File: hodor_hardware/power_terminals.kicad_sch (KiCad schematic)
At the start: 60 parts, among them J1 Screw_Terminal_01x02, Q1 SiS443DN, T1 GND, T10 V_{BUS}, T11 3V3, T12 5V, T14 V_{BUS}_SENSE, T32 GND, T6 V_{DC}_SENSE, T9 V_{DC}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

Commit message: Schematic finished
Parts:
- removed C62: 100n, Capacitor_SMD:C_0402_1005Metric, symbol Device:C
- added C66, C67, C68, C69, C70: 10uF, Capacitor_SMD:C_0805_2012Metric, symbol Device:C
- C10, C38, C58, C65: value 100n -> 100nF
- C45: value 100n -> 4.7uF/50V; footprint Capacitor_SMD:C_0402_1005Metric -> Capacitor_SMD:C_1206_3216Metric
- C46, C59: value 100n -> 100n/50V; footprint Capacitor_SMD:C_0402_1005Metric -> Capacitor_SMD:C_0603_1608Metric
- C57: value 100n -> 6.8nF
- C60: value 100n -> 15nF
- C61: value 100n -> 10p
- C64: footprint Capacitor_SMD:C_1206_3216Metric -> Capacitor_SMD:C_0805_2012Metric
- D16: value D_Schottky -> PMEG4050; footprint (none) -> Diode_SMD:D_SMB
- L13: value L_Iron -> 27uH; footprint (none) -> Inductor_SMD:L_12x12mm_H6mm
- R22, R42: value 2k -> 2.2k
- R41: value 18.2k -> 100k
- R73: value 18.2k -> 52.3k
- R74: value 18.2k -> 10k
- R75: value 18.2k -> 205k
- T1, T10, T11, T12, T14, T32, T6, T9: now left out of the parts list
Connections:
- net +5V: now also C66.1, C67.1, C68.1, C69.1, C70.1
- net GND: now also C66.2, C67.2, C68.2, C69.2, C70.2
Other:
- note added: "DC/DC converters for logic supply"
- note removed: "WARNING: R/C Values not calculated yet!"
- moved on the sheet: C45, C46, C57, C58, C59, C60, C61, C63, C64, C65, D16, L13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

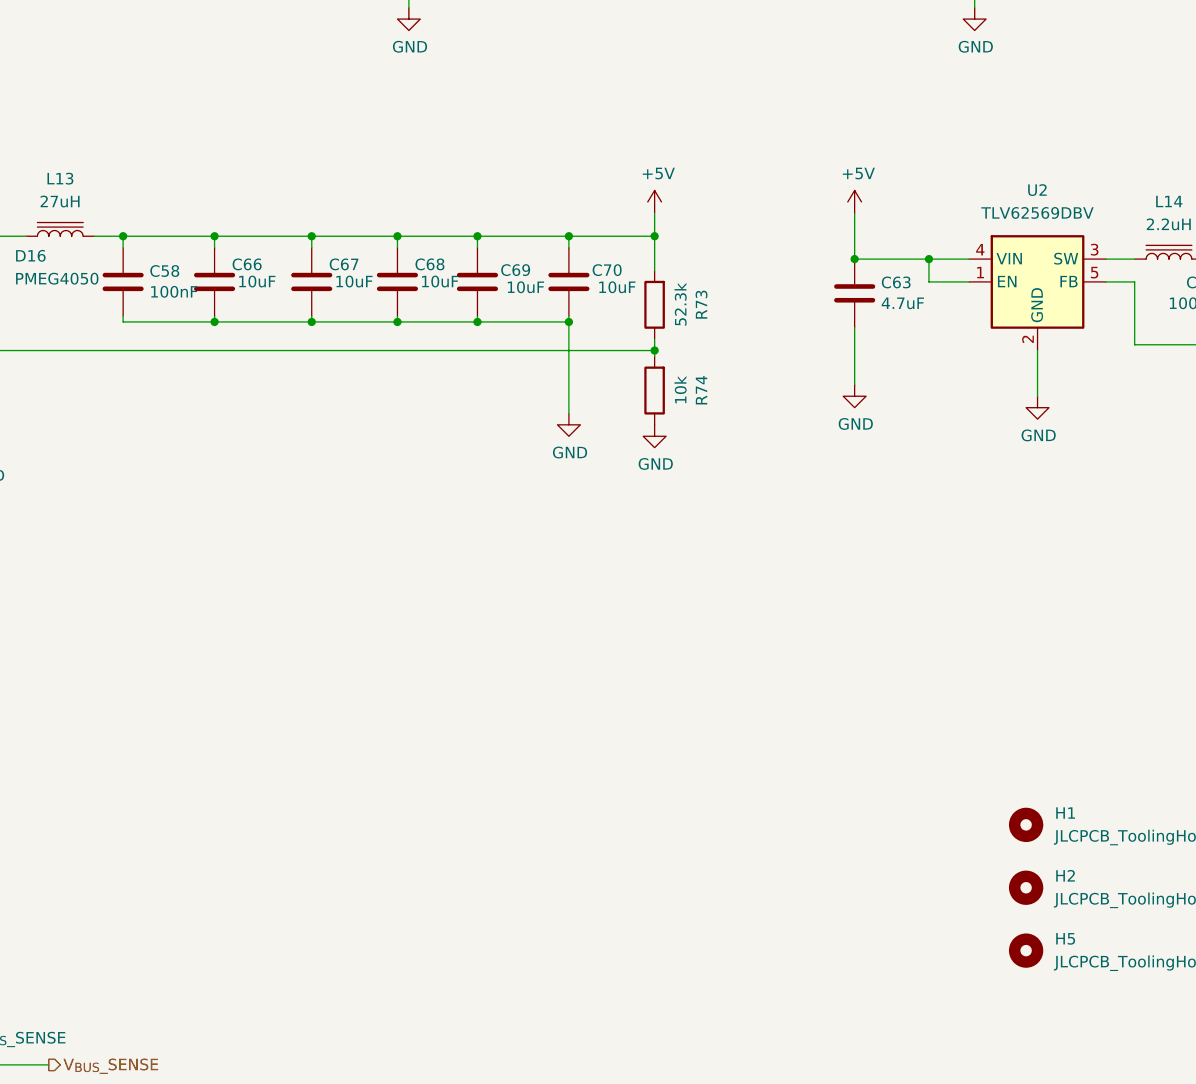
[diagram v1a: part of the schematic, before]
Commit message: Added USB switchover function for 5V
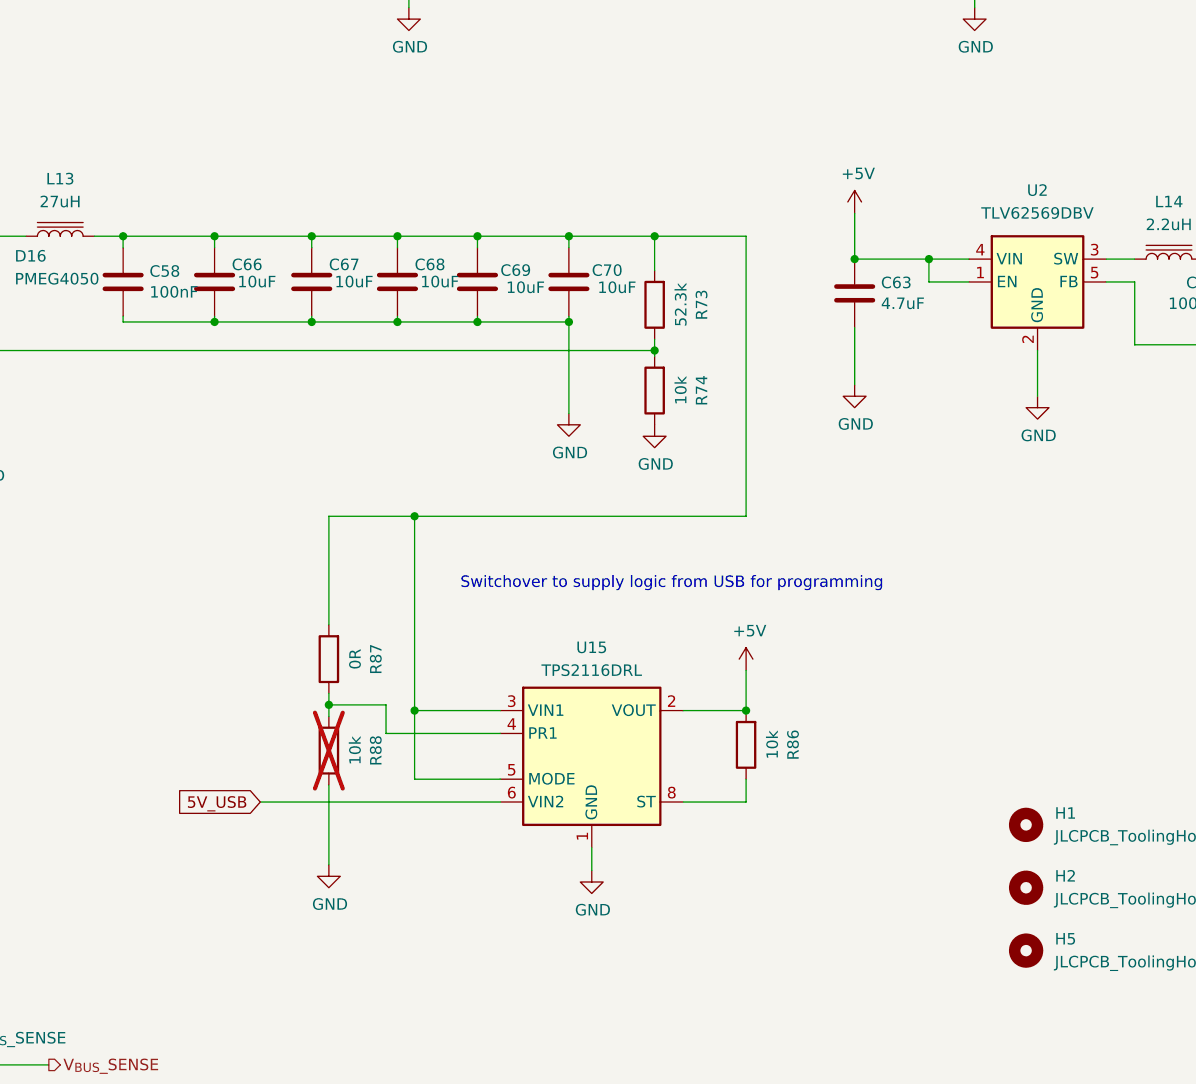
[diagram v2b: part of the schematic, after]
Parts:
- added R86, R88: 10k, Resistor_SMD:R_0402_1005Metric, symbol Device:R
- added R87: 0R, Resistor_SMD:R_0402_1005Metric, symbol Device:R
- added U15: TPS2116DRL, Package_TO_SOT_SMD:SOT-583-8, symbol Power_Management:TPS2116DRL
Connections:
- net +5V: now also R86.2, U15.2 (VOUT), U15.7 (VOUT); no longer C58.1, C66.1, C67.1, C68.1, C69.1, C70.1, L13.2, R73.2
- net GND: now also R88.1, U15.1 (GND)
- new net: R86.1, U15.8 (ST)
- new net: C58.1, C66.1, C67.1, C68.1, C69.1, C70.1, L13.2, R73.2, R87.2, U15.3 (VIN1), U15.5 (MODE)
- new net: R87.1, R88.2, U15.4 (PR1)
- new net 5V_USB: U15.6 (VIN2)
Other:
- note added: "Switchover to supply logic from USB for programming"

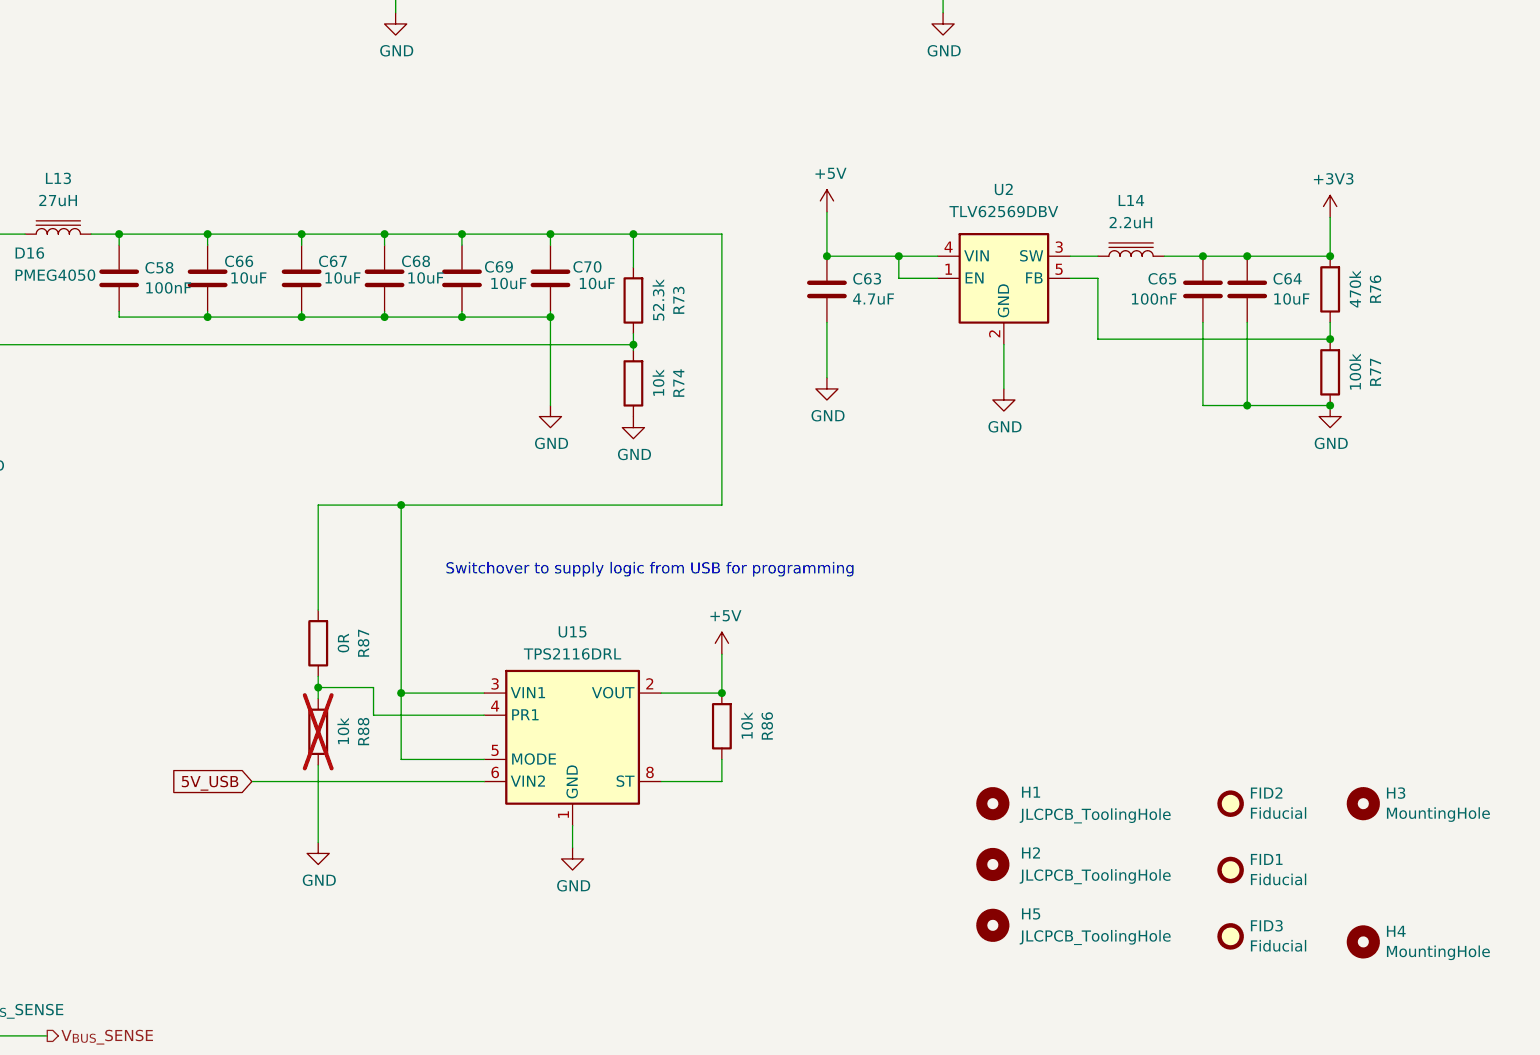
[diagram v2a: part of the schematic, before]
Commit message: Reworked into 2 PCBs
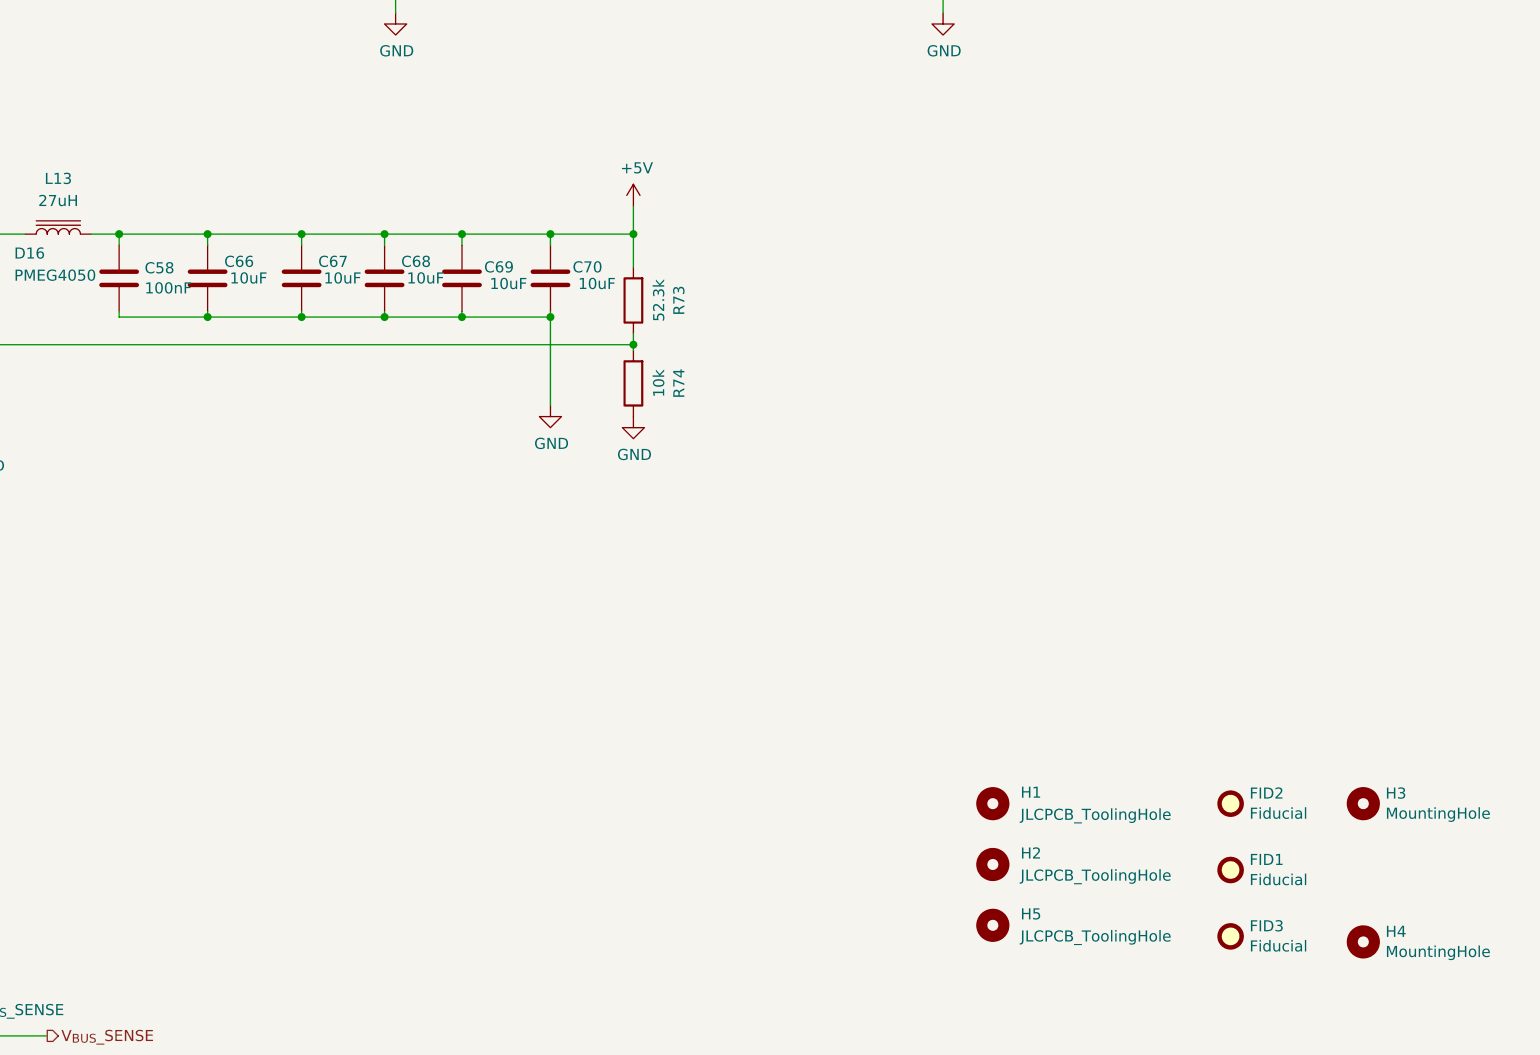
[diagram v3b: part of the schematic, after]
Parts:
- removed C63: 4.7uF, Capacitor_SMD:C_1206_3216Metric, symbol Device:C
- removed C64: 10uF, Capacitor_SMD:C_0805_2012Metric, symbol Device:C
- removed C65: 100nF, Capacitor_SMD:C_0402_1005Metric, symbol Device:C
- removed L14: 2.2uH, Inductor_SMD:L_1812_4532Metric, symbol Device:L_Iron
- removed R76: 470k, Resistor_SMD:R_0402_1005Metric, symbol Device:R
- removed R77: 100k, Resistor_SMD:R_0402_1005Metric, symbol Device:R
- removed R86, R88: 10k, Resistor_SMD:R_0402_1005Metric, symbol Device:R
- removed R87: 0R, Resistor_SMD:R_0402_1005Metric, symbol Device:R
- removed U15: TPS2116DRL, Package_TO_SOT_SMD:SOT-583-8, symbol Power_Management:TPS2116DRL
- removed U2: TLV62569DBV, Package_TO_SOT_SMD:SOT-23-5, symbol Regulator_Switching:TLV62569DBV
- J1: footprint TerminalBlock_Phoenix:TerminalBlock_Phoenix_PT-1,5-2-3.5-H_1x02_P3.50mm_Horizontal -> TerminalBlock_Phoenix:TerminalBlock_Phoenix_MKDS-1,5-2_1x02_P5.00mm_Horizontal
- L13: footprint Inductor_SMD:L_12x12mm_H6mm -> Inductor_SMD:L_Wuerth_WE-PD-Typ-7345
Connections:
- net +5V: now also C58.1, C66.1, C67.1, C68.1, C69.1, C70.1, L13.2, R73.2
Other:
- note removed: "Switchover to supply logic from USB for programming"

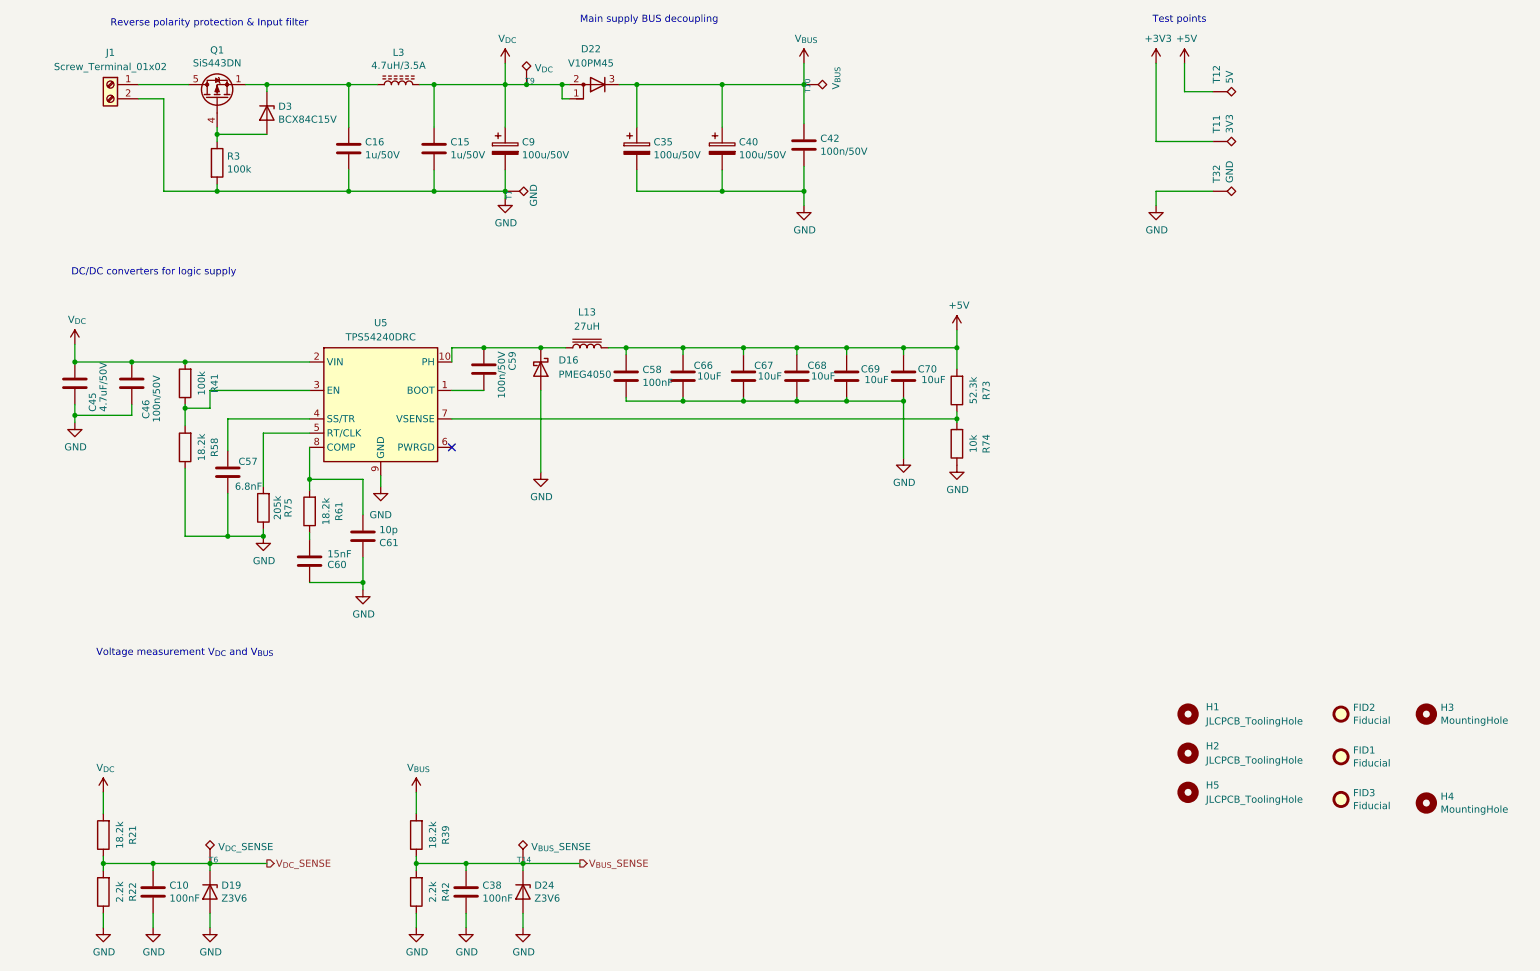
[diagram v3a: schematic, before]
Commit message: Finished schematic and initial placement on PCB
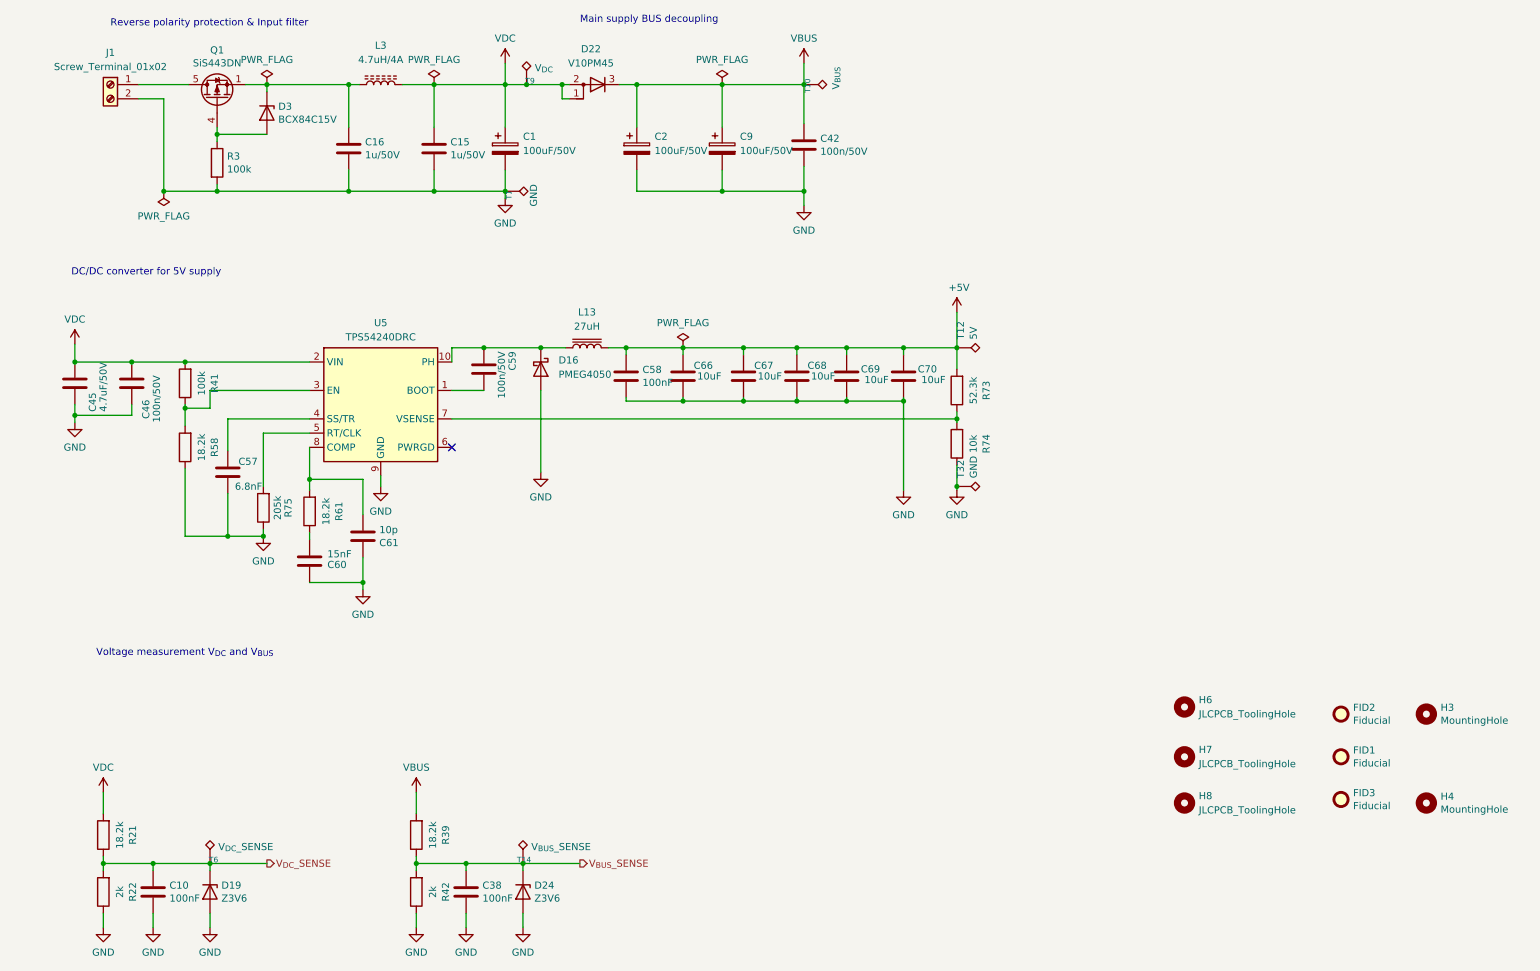
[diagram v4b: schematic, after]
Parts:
- removed C35, C40, C9: 100u/50V, Capacitor_SMD:CP_Elec_8x10.5, symbol Hodor-rescue:C_Polarized-Device
- removed H1, H2, H5: JLCPCB_ToolingHole, mm_parts_footprints:JLCPCB_ToolingHole, symbol mm_parts:JLCPCB_ToolingHole
- removed L3: 4.7uH/3.5A, Inductor_SMD:L_Wuerth_HCI-7030, symbol Hodor-rescue:L_Ferrite-Device
- removed T11: 3V3, TestPoint:TestPoint_Pad_D1.0mm, symbol Connector:TestPoint_Alt
- added C1, C2, C9: 100uF/50V, Capacitor_SMD:C_Elec_8x10.2, symbol Device:C_Polarized
- added H6, H7, H8: JLCPCB_ToolingHole, hodor_footprints:JLCPCB_ToolingHole, symbol hodor_custom_parts:JLCPCB_ToolingHole
- added L3: 4.7uH/4A, Inductor_SMD:L_Wuerth_MAPI-4020, symbol Device:L_Ferrite
- R22, R42: value 2.2k -> 2k
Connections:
- net GND: now also C1.2, C2.2, C9.2
- net at C16.1, D3.1 (K), Q1.1 (S)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: now also L3.1
- net V_{BUS} renamed VBUS
- net VBUS: now also C2.1, C9.1
- net V_{DC} renamed VDC
- net VDC: now also C1.1, L3.2
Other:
- note added: "DC/DC converter for 5V supply"
- note removed: "DC/DC converters for logic supply"
- note removed: "Test points"
- moved on the sheet: T12, T32
